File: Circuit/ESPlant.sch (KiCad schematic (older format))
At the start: 44 parts, among them P101 CONN_DIGITAL, P102 CONN_ANALOG, P103 CONN_SERIAL, P104 CONN_I2C, P105 SOLAR, P106 USB_5PIN_SHELL, P107 CONN_PWR3, P108 CONN_PWR2, P109 CONN_PWR, P110 CONN_01X05, P111 UV, P112 TEMP, P113 NEOPIXEL, P114 PIR, Q101 FDN340P, SW101 RESET, SW102 PRGM, SW103 RESET, U101 STM32F042F, U103 ESP-12E

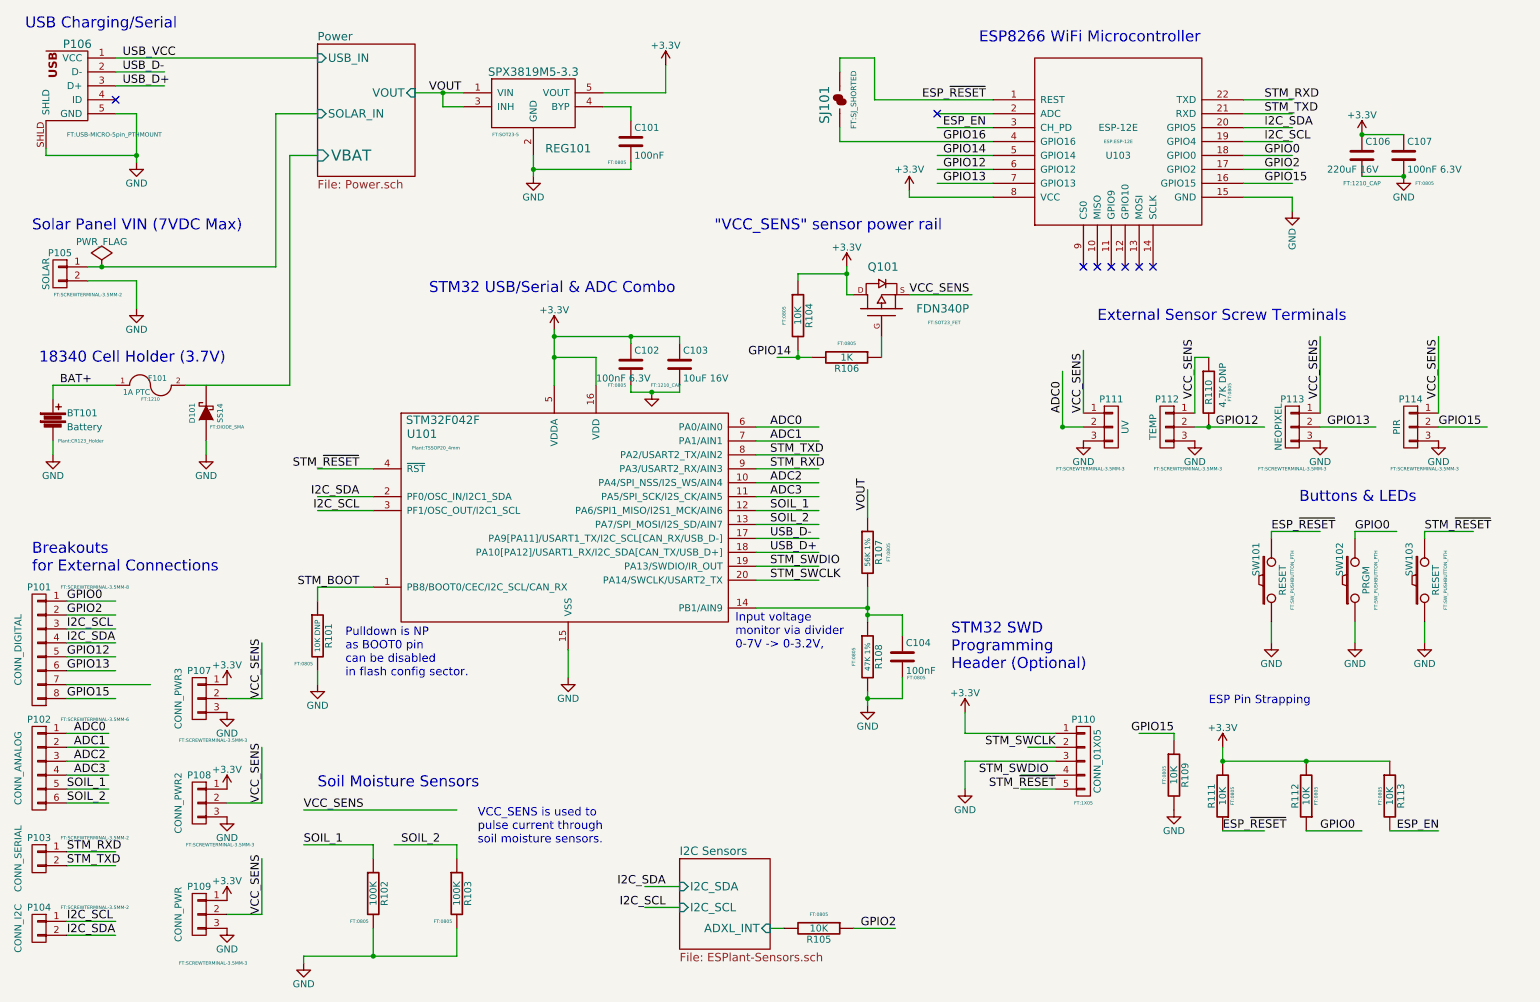
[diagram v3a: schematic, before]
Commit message: Updated footprints for connectors
Removed Surplus power.
Added connectors for soil sensor.
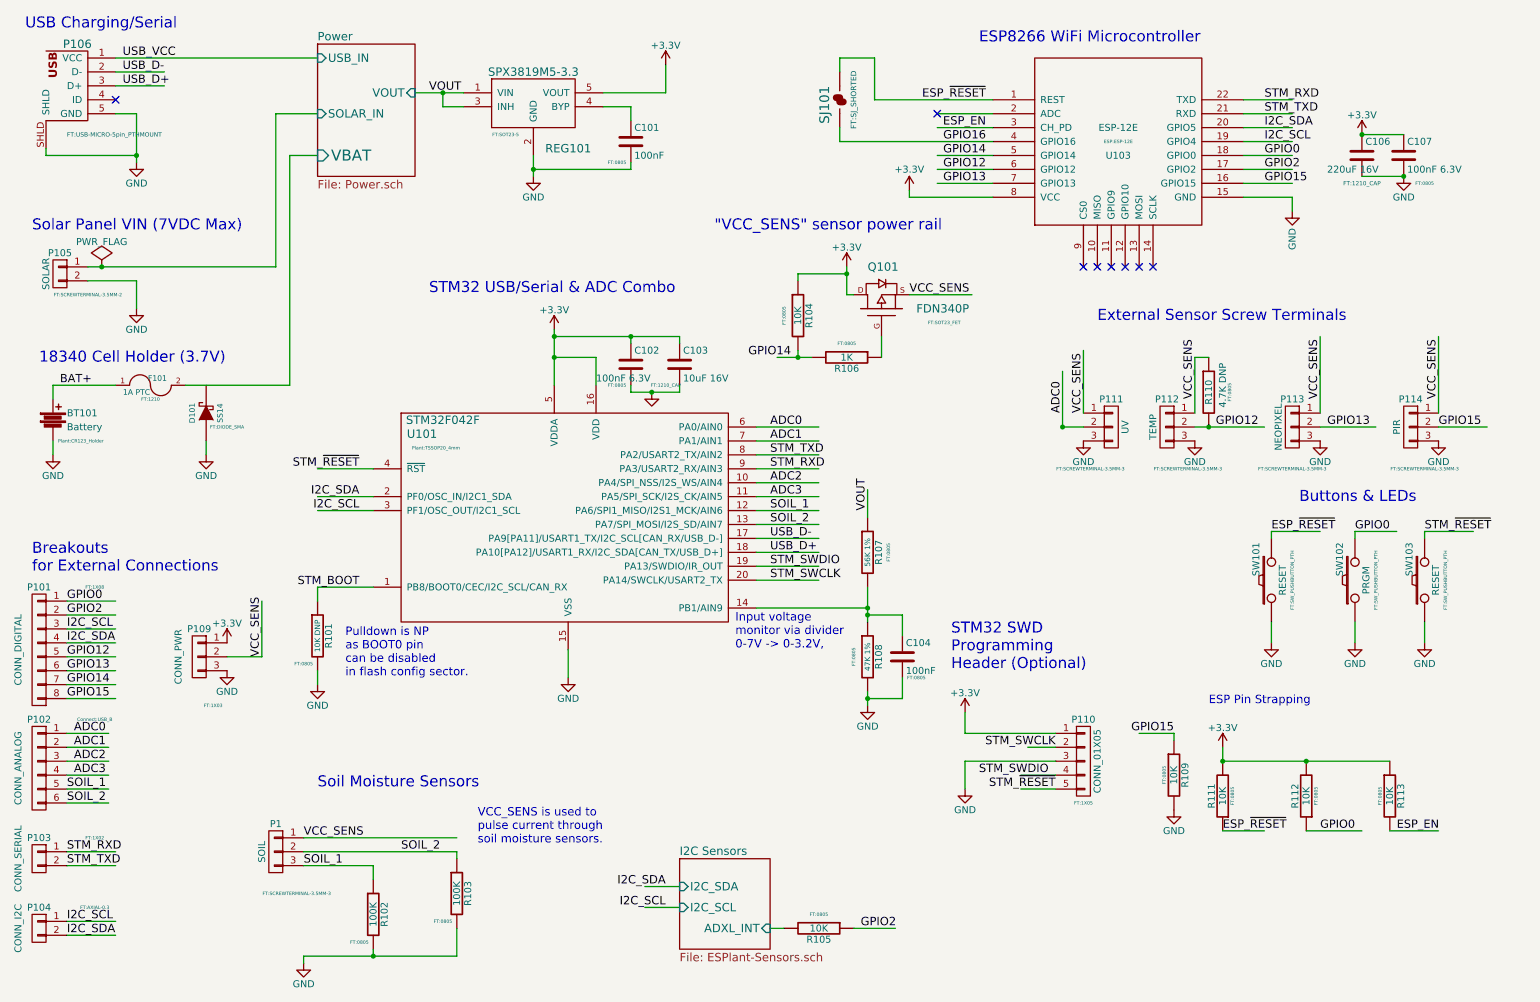
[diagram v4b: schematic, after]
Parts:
- removed P107: CONN_PWR3, FT:SCREWTERMINAL-3.5MM-3, symbol CONN_01X03
- removed P108: CONN_PWR2, FT:SCREWTERMINAL-3.5MM-3, symbol CONN_01X03
- added P1: SOIL, FT:SCREWTERMINAL-3.5MM-3, symbol CONN_01X03
- P101: footprint FT:SCREWTERMINAL-3.5MM-8 -> FT:1X08
- P102: footprint FT:SCREWTERMINAL-3.5MM-6 -> Connect:USB_B
- P103: footprint FT:SCREWTERMINAL-3.5MM-2 -> FT:1X02
- P104: footprint FT:SCREWTERMINAL-3.5MM-2 -> FT:AXIAL-0.3
- P109: footprint FT:SCREWTERMINAL-3.5MM-3 -> FT:1X03
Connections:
- wire segments 167 -> 179
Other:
- moved on the sheet: P109, R102
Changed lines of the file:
@@
 L R R102
 U 1 1 564D9EB2
-P 3150 6850
-F 0 "R102" V 3230 6850 50  0000 C CNN
-F 1 "100K" V 3150 6850 50  0000 C CNN
-F 2 "FT:0805" H 3050 6650 24  0000 C CNN
-F 3 "" H 3150 6850 60  0000 C CNN
-	1    3150 6850
-	1    0    0    -1
-$EndComp
-Text Label 2650 6500 0    60   ~ 0
+P 3150 7000
+F 0 "R102" V 3230 7000 50  0000 C CNN
+F 1 "100K" V 3150 7000 50  0000 C CNN
+F 2 "FT:0805" H 3050 6800 24  0000 C CNN
+F 3 "" H 3150 7000 60  0000 C CNN
+	1    3150 7000
+	1    0    0    -1
+$EndComp
+Text Label 2650 6650 0    60   ~ 0
 SOIL_1
 Text Label 6000 4100 0    60   ~ 0
@@
 	1    0    0    -1
 $EndComp
-Text Label 3350 6500 0    60   ~ 0
+Text Label 3350 6550 0    60   ~ 0
 SOIL_2
 Text Label 5250 6800 2    60   ~ 0
@@
 Text Label 7550 1550 2    60   ~ 0
 GPIO14
-Text Label 2650 6250 0    60   ~ 0
+Text Label 2650 6450 0    60   ~ 0
 VCC_SENS
 $Comp
@@
 VCC_SENS
 Wire Wire Line
-	3750 6500 3300 6500
-Wire Wire Line
-	3750 6600 3750 6500
+	2650 6550 3750 6550
+Wire Wire Line
+	3750 6550 3750 6600
 Wire Wire Line
 	3750 7300 3750 7100
 Wire Wire Line
-	2650 7300 3750 7300
+	2650 7300 3150 7300
+Wire Wire Line
+	3150 7300 3750 7300
 Wire Wire Line
 	10800 3400 10800 2850
@@
 	6550 2550 6600 2550
 Wire Wire Line
-	6550 2350 6550 2550
+	6550 2350 6550 2400
+Wire Wire Line
+	6550 2400 6550 2550
 Wire Wire Line
 	6800 3000 6800 2850
@@
 	7000 2550 7450 2550
 Wire Wire Line
-	9050 3500 9550 3500
+	9050 3500 9150 3500
+Wire Wire Line
+	9150 3500 9550 3500
 Wire Wire Line
 	9950 3500 10350 3500
@@
 	5350 3250 5350 3200
 Wire Wire Line
-	5000 3250 5350 3250
+	5000 3250 5150 3250
+Wire Wire Line
+	5150 3250 5350 3250
 Connection ~ 5000 2850
 Wire Wire Line
@@
 	5000 2850 5000 2900
 Wire Wire Line
-	4450 2850 5350 2850
+	4450 2850 5000 2850
+Wire Wire Line
+	5000 2850 5350 2850
 Wire Wire Line
 	7400 5900 7400 6100
@@
 Connection ~ 4450 3000
 Wire Wire Line
-	4450 2800 4450 3200
+	4450 2800 4450 2850
+Wire Wire Line
+	4450 2850 4450 3000
+Wire Wire Line
+	4450 3000 4450 3200
 Wire Wire Line
 	4750 3000 4450 3000
@@
 	6950 4850 6950 5000
 Wire Wire Line
-	6700 5400 6700 5500
+	6700 5400 6700 5450
+Wire Wire Line
+	6700 5450 6700 5500
 Connection ~ 6700 4800
 Wire Wire Line
@@
 Connection ~ 3150 7300
 Wire Wire Line
-	2650 6500 3150 6500
-Wire Wire Line
-	2650 6250 3750 6250
+	2650 6650 3150 6650
+Wire Wire Line
+	2650 6450 3750 6450
 Wire Wire Line
 	6500 1350 6500 1450
@@
 	5350 6800 5100 6800
 Wire Wire Line
-	3150 7100 3150 7300
-Wire Wire Line
-	3150 6500 3150 6600
+	3150 7250 3150 7300
+Wire Wire Line
+	3150 6650 3150 6750
 Wire Wire Line
 	8900 5700 8650 5700
@@
 	8900 5750 8900 5700
 Wire Wire Line
-	6700 4650 6700 4900
+	6700 4650 6700 4800
+Wire Wire Line
+	6700 4800 6700 4850
+Wire Wire Line
+	6700 4850 6700 4900
 Wire Wire Line
 	6700 4150 6700 3950
@@
 	2450 1250 2750 1250
 Wire Wire Line
-	4300 1550 4300 1700
+	4300 1550 4300 1650
+Wire Wire Line
+	4300 1650 4300 1700
 Wire Wire Line
 	5250 1100 5250 900
@@
 	3800 1200 3650 1200
 Wire Wire Line
-	3450 1100 3800 1100
+	3450 1100 3650 1100
+Wire Wire Line
+	3650 1100 3800 1100
 Wire Wire Line
 	1450 2450 1450 2650
@@
 	1100 2450 1450 2450
 Wire Wire Line
-	1100 2350 2450 2350
+	1100 2350 1200 2350
+Wire Wire Line
+	1200 2350 2450 2350
 Wire Wire Line
 	2450 2350 2450 1250
@@
 	1450 1250 1300 1250
 Wire Wire Line
-	1450 1250 1450 1600
+	1450 1250 1450 1550
+Wire Wire Line
+	1450 1550 1450 1600
 Wire Wire Line
 	7600 1750 7200 1750
@@
 Connection ~ 9250 5900
 Wire Wire Line
-	9250 5900 10450 5900
+	9250 5900 9850 5900
+Wire Wire Line
+	9850 5900 10450 5900
 Wire Wire Line
 	9250 5800 9250 5900
@@
 L CONN_01X03 P109
 U 1 1 565C0856
-P 1900 7000
-F 0 "P109" H 1900 7200 50  0000 C CNN
-F 1 "CONN_PWR" V 2050 7000 50  0000 C CNN
-F 2 "FT:SCREWTERMINAL-3.5MM-3" H 1800 6650 24  0000 C CNN
-F 3 "" H 1900 7000 60  0000 C CNN
-	1    1900 7000
+P 1900 5150
+F 0 "P109" H 1900 5350 50  0000 C CNN
+F 1 "CONN_PWR" V 2050 5150 50  0000 C CNN
+F 2 "FT:1X03" H 1800 4800 24  0000 C CNN
+F 3 "" H 1900 5150 60  0000 C CNN
+	1    1900 5150
 	-1   0    0    -1
 $EndComp
@@
 L +3.3V #PWR029
 U 1 1 565C1114
-P 2100 6900
-F 0 "#PWR029" H 2100 6750 50  0001 C CNN
-F 1 "+3.3V" H 2100 7040 50  0000 C CNN
-F 2 "" H 2100 6900 60  0000 C CNN
-F 3 "" H 2100 6900 60  0000 C CNN
-	1    2100 6900
+P 2100 5050
+F 0 "#PWR029" H 2100 4900 50  0001 C CNN
+F 1 "+3.3V" H 2100 5190 50  0000 C CNN
+F 2 "" H 2100 5050 60  0000 C CNN
+F 3 "" H 2100 5050 60  0000 C CNN
+	1    2100 5050
 	1    0    0    -1
 $EndComp
@@
 L GND #PWR030
 U 1 1 565C1810
-P 2100 7100
-F 0 "#PWR030" H 2100 6850 50  0001 C CNN
-F 1 "GND" H 2100 6950 50  0000 C CNN
-F 2 "" H 2100 7100 60  0000 C CNN
-F 3 "" H 2100 7100 60  0000 C CNN
-	1    2100 7100
-	1    0    0    -1
-$EndComp
-Text Label 2350 7000 1    60   ~ 0
+P 2100 5250
+F 0 "#PWR030" H 2100 5000 50  0001 C CNN
+F 1 "GND" H 2100 5100 50  0000 C CNN
+F 2 "" H 2100 5250 60  0000 C CNN
+F 3 "" H 2100 5250 60  0000 C CNN
+	1    2100 5250
+	1    0    0    -1
+$EndComp
+Text Label 2350 5150 1    60   ~ 0
 VCC_SENS
 $Comp
@@
 F 0 "P102" H 750 6300 50  0000 C CNN
 F 1 "CONN_ANALOG" V 900 5950 50  0000 C CNN
-F 2 "FT:SCREWTERMINAL-3.5MM-6" H 350 6300 24  0000 C CNN
+F 2 "Connect:USB_B" H 350 6300 24  0000 C CNN
 F 3 "" H 750 5950 60  0000 C CNN
 	1    750  5950
@@
 F 0 "P103" H 750 6750 50  0000 C CNN
 F 1 "CONN_SERIAL" V 900 6600 50  0000 C CNN
-F 2 "FT:SCREWTERMINAL-3.5MM-2" H 350 6750 24  0000 C CNN
+F 2 "FT:1X02" H 350 6750 24  0000 C CNN
 F 3 "" H 750 6600 60  0000 C CNN
 	1    750  6600
@@
 F 0 "P101" H 750 5550 50  0000 C CNN
 F 1 "CONN_DIGITAL" V 900 5100 50  0000 C CNN
-F 2 "FT:SCREWTERMINAL-3.5MM-8" H 350 5550 24  0000 C CNN
+F 2 "FT:1X08" H 350 5550 24  0000 C CNN
 F 3 "" H 750 5100 60  0000 C CNN
 	1    750  5100
@@
 	950  5250 1300 5250
 Wire Wire Line
-	950  5350 1550 5350
+	950  5350 1300 5350
 Wire Wire Line
 	950  5450 1300 5450
@@
 F 0 "P104" H 750 7250 50  0000 C CNN
 F 1 "CONN_I2C" V 900 7100 50  0000 C CNN
-F 2 "FT:SCREWTERMINAL-3.5MM-2" H 350 7250 24  0000 C CNN
+F 2 "FT:AXIAL-0.3" H 350 7250 24  0000 C CNN
 F 3 "" H 750 7100 60  0000 C CNN
 	1    750  7100
@@
 	950  7150 1300 7150
 Wire Wire Line
-	2100 7000 2350 7000
-Wire Wire Line
-	2350 7000 2350 6600
-$Comp
-L CONN_01X03 P107
-U 1 1 565CBC72
-P 1900 5450
-F 0 "P107" H 1900 5650 50  0000 C CNN
-F 1 "CONN_PWR3" V 2050 5450 50  0000 C CNN
-F 2 "FT:SCREWTERMINAL-3.5MM-3" H 1800 5150 24  0000 C CNN
-F 3 "" H 1900 5450 60  0000 C CNN
-	1    1900 5450
-	-1   0    0    -1
-$EndComp
-$Comp
-L +3.3V #PWR031
-U 1 1 565CBC78
-P 2100 5350
-F 0 "#PWR031" H 2100 5200 50  0001 C CNN
-F 1 "+3.3V" H 2100 5490 50  0000 C CNN
-F 2 "" H 2100 5350 60  0000 C CNN
-F 3 "" H 2100 5350 60  0000 C CNN
-	1    2100 5350
-	1    0    0    -1
-$EndComp
-$Comp
-L GND #PWR032
-U 1 1 565CBC7E
-P 2100 5550
-F 0 "#PWR032" H 2100 5300 50  0001 C CNN
-F 1 "GND" H 2100 5400 50  0000 C CNN
-F 2 "" H 2100 5550 60  0000 C CNN
-F 3 "" H 2100 5550 60  0000 C CNN
-	1    2100 5550
-	1    0    0    -1
-$EndComp
-Text Label 2350 5450 1    60   ~ 0
-VCC_SENS
-Wire Wire Line
-	2100 5450 2350 5450
-Wire Wire Line
-	2350 5450 2350 5050
-$Comp
-L CONN_01X03 P108
-U 1 1 565CC26E
-P 1900 6200
-F 0 "P108" H 1900 6400 50  0000 C CNN
-F 1 "CONN_PWR2" V 2050 6200 50  0000 C CNN
-F 2 "FT:SCREWTERMINAL-3.5MM-3" H 1750 5900 24  0000 C CNN
-F 3 "" H 1900 6200 60  0000 C CNN
-	1    1900 6200
-	-1   0    0    -1
-$EndComp
-$Comp
-L +3.3V #PWR033
-U 1 1 565CC274
-P 2100 6100
-F 0 "#PWR033" H 2100 5950 50  0001 C CNN
-F 1 "+3.3V" H 2100 6240 50  0000 C CNN
-F 2 "" H 2100 6100 60  0000 C CNN
-F 3 "" H 2100 6100 60  0000 C CNN
-	1    2100 6100
-	1    0    0    -1
-$EndComp
-$Comp
-L GND #PWR034
-U 1 1 565CC27A
-P 2100 6300
-F 0 "#PWR034" H 2100 6050 50  0001 C CNN
-F 1 "GND" H 2100 6150 50  0000 C CNN
-F 2 "" H 2100 6300 60  0000 C CNN
-F 3 "" H 2100 6300 60  0000 C CNN
-	1    2100 6300
-	1    0    0    -1
-$EndComp
-Text Label 2350 6200 1    60   ~ 0
-VCC_SENS
-Wire Wire Line
-	2100 6200 2350 6200
-Wire Wire Line
-	2350 6200 2350 5800
+	2100 5150 2350 5150
+Wire Wire Line
+	2350 5150 2350 4750
 $Comp
 L FUSE F101
@@
 $EndComp
 $Comp
-L GND #PWR035
+L GND #PWR031
 U 1 1 565D25EB
 P 1950 3700
-F 0 "#PWR035" H 1950 3450 50  0001 C CNN
+F 0 "#PWR031" H 1950 3450 50  0001 C CNN
 F 1 "GND" H 1950 3550 50  0000 C CNN
 F 2 "" H 1950 3700 60  0000 C CNN
@@
 $EndComp
 Wire Wire Line
-	6050 3000 6300 3000
+	6050 3000 6200 3000
+Wire Wire Line
+	6200 3000 6300 3000
 Wire Wire Line
 	6200 3000 6200 2950
@@
 Text Notes 8350 2750 0    79   ~ 0
 External Sensor Screw Terminals
+$Comp
+L CONN_01X03 P1
+U 1 1 565889BC
+P 2450 6550
+F 0 "P1" H 2450 6750 50  0000 C CNN
+F 1 "SOIL" V 2550 6550 50  0000 C CNN
+F 2 "FT:SCREWTERMINAL-3.5MM-3" H 2300 6250 24  0000 C CNN
+F 3 "" H 2450 6550 60  0000 C CNN
+	1    2450 6550
+	-1   0    0    -1
+$EndComp
+Text Label 950  5350 0    60   ~ 0
+GPIO14
 $EndSCHEMATC

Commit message: Fuse missing connection
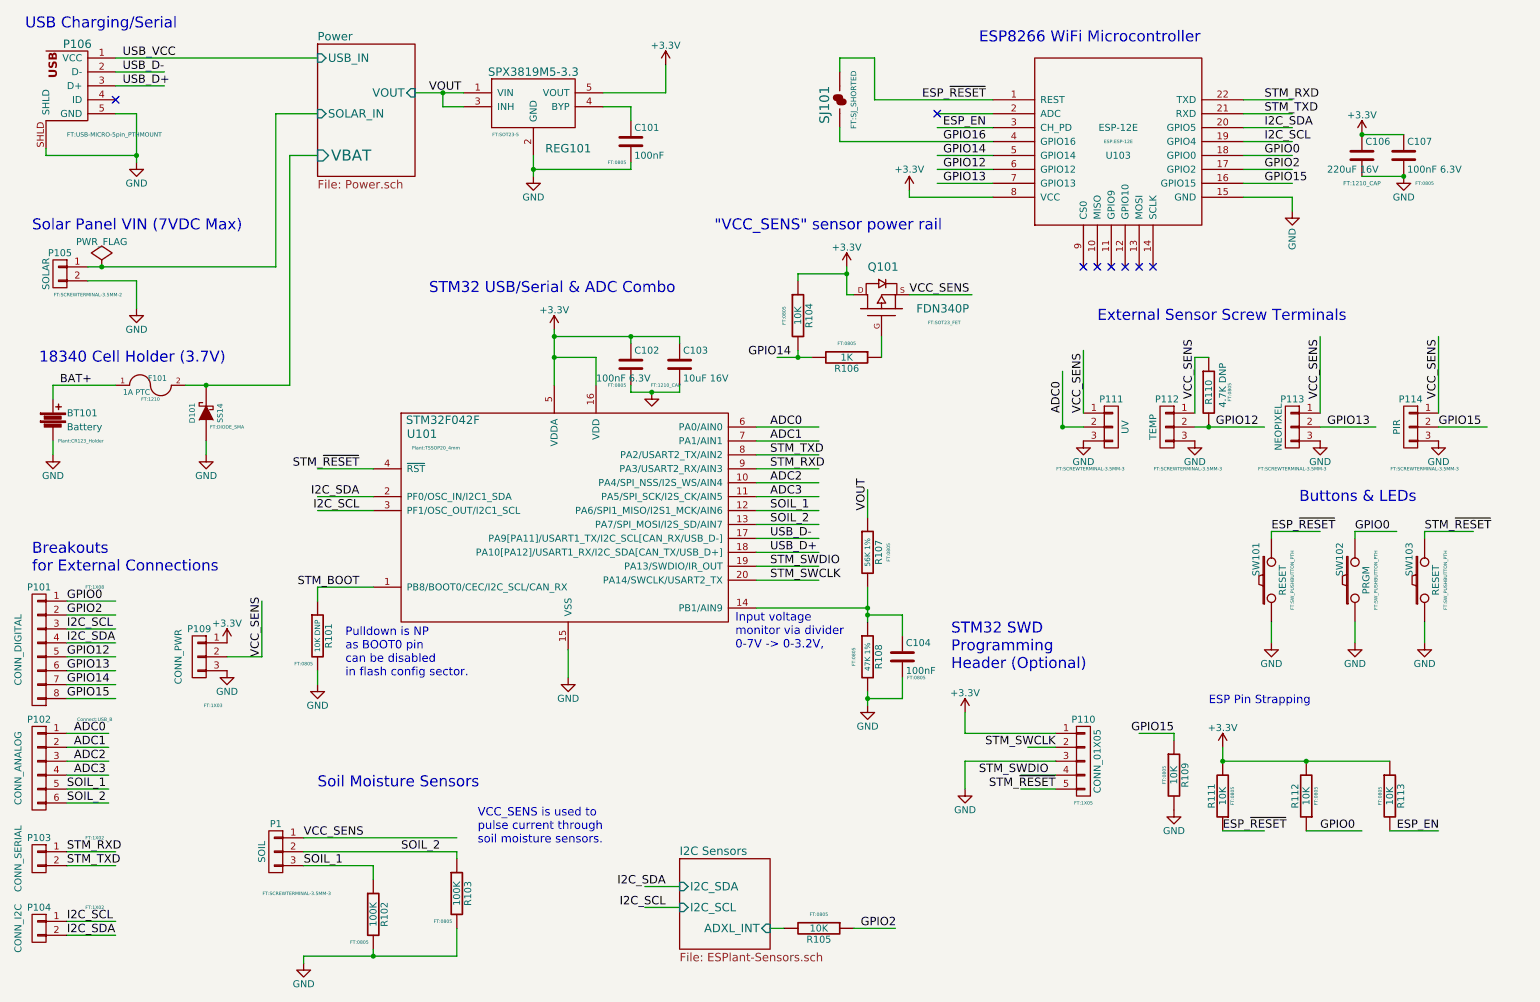
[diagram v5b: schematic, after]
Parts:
- P104: footprint FT:AXIAL-0.3 -> FT:1X02
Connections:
- wire segments 179 -> 163
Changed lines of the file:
@@
 	3750 7300 3750 7100
 Wire Wire Line
-	2650 7300 3150 7300
-Wire Wire Line
-	3150 7300 3750 7300
+	2650 7300 3750 7300
 Wire Wire Line
 	10800 3400 10800 2850
@@
 	6550 2550 6600 2550
 Wire Wire Line
-	6550 2350 6550 2400
-Wire Wire Line
-	6550 2400 6550 2550
+	6550 2350 6550 2550
 Wire Wire Line
 	6800 3000 6800 2850
@@
 	7000 2550 7450 2550
 Wire Wire Line
-	9050 3500 9150 3500
-Wire Wire Line
-	9150 3500 9550 3500
+	9050 3500 9550 3500
 Wire Wire Line
 	9950 3500 10350 3500
@@
 	5350 3250 5350 3200
 Wire Wire Line
-	5000 3250 5150 3250
-Wire Wire Line
-	5150 3250 5350 3250
+	5000 3250 5350 3250
 Connection ~ 5000 2850
 Wire Wire Line
@@
 	5000 2850 5000 2900
 Wire Wire Line
-	4450 2850 5000 2850
-Wire Wire Line
-	5000 2850 5350 2850
+	4450 2850 5350 2850
 Wire Wire Line
 	7400 5900 7400 6100
@@
 Connection ~ 4450 3000
 Wire Wire Line
-	4450 2800 4450 2850
-Wire Wire Line
-	4450 2850 4450 3000
-Wire Wire Line
-	4450 3000 4450 3200
+	4450 2800 4450 3200
 Wire Wire Line
 	4750 3000 4450 3000
@@
 	6950 4850 6950 5000
 Wire Wire Line
-	6700 5400 6700 5450
-Wire Wire Line
-	6700 5450 6700 5500
+	6700 5400 6700 5500
 Connection ~ 6700 4800
 Wire Wire Line
@@
 	8900 5750 8900 5700
 Wire Wire Line
-	6700 4650 6700 4800
-Wire Wire Line
-	6700 4800 6700 4850
-Wire Wire Line
-	6700 4850 6700 4900
+	6700 4650 6700 4900
 Wire Wire Line
 	6700 4150 6700 3950
@@
 	2450 1250 2750 1250
 Wire Wire Line
-	4300 1550 4300 1650
-Wire Wire Line
-	4300 1650 4300 1700
+	4300 1550 4300 1700
 Wire Wire Line
 	5250 1100 5250 900
@@
 	3800 1200 3650 1200
 Wire Wire Line
-	3450 1100 3650 1100
-Wire Wire Line
-	3650 1100 3800 1100
+	3450 1100 3800 1100
 Wire Wire Line
 	1450 2450 1450 2650
@@
 	1100 2450 1450 2450
 Wire Wire Line
-	1100 2350 1200 2350
-Wire Wire Line
-	1200 2350 2450 2350
+	1100 2350 2450 2350
 Wire Wire Line
 	2450 2350 2450 1250
@@
 	1450 1250 1300 1250
 Wire Wire Line
-	1450 1250 1450 1550
-Wire Wire Line
-	1450 1550 1450 1600
+	1450 1250 1450 1600
 Wire Wire Line
 	7600 1750 7200 1750
@@
 Connection ~ 9250 5900
 Wire Wire Line
-	9250 5900 9850 5900
-Wire Wire Line
-	9850 5900 10450 5900
+	9250 5900 10450 5900
 Wire Wire Line
 	9250 5800 9250 5900
@@
 F 0 "P104" H 750 7250 50  0000 C CNN
 F 1 "CONN_I2C" V 900 7100 50  0000 C CNN
-F 2 "FT:AXIAL-0.3" H 350 7250 24  0000 C CNN
+F 2 "FT:1X02" H 350 7250 24  0000 C CNN
 F 3 "" H 750 7100 60  0000 C CNN
 	1    750  7100
@@
 $EndComp
 Wire Wire Line
-	6050 3000 6200 3000
-Wire Wire Line
-	6200 3000 6300 3000
+	6050 3000 6300 3000
 Wire Wire Line
 	6200 3000 6200 2950
@@
 Text Label 950  5350 0    60   ~ 0
 GPIO14
+Connection ~ 1950 3200
 $EndSCHEMATC
